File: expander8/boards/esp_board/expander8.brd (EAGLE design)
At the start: 68.6 x 46.7 mm, 63 parts, among them IC1 STM32F10XCXT6, IC2 78L05F, J1 DCJ0202

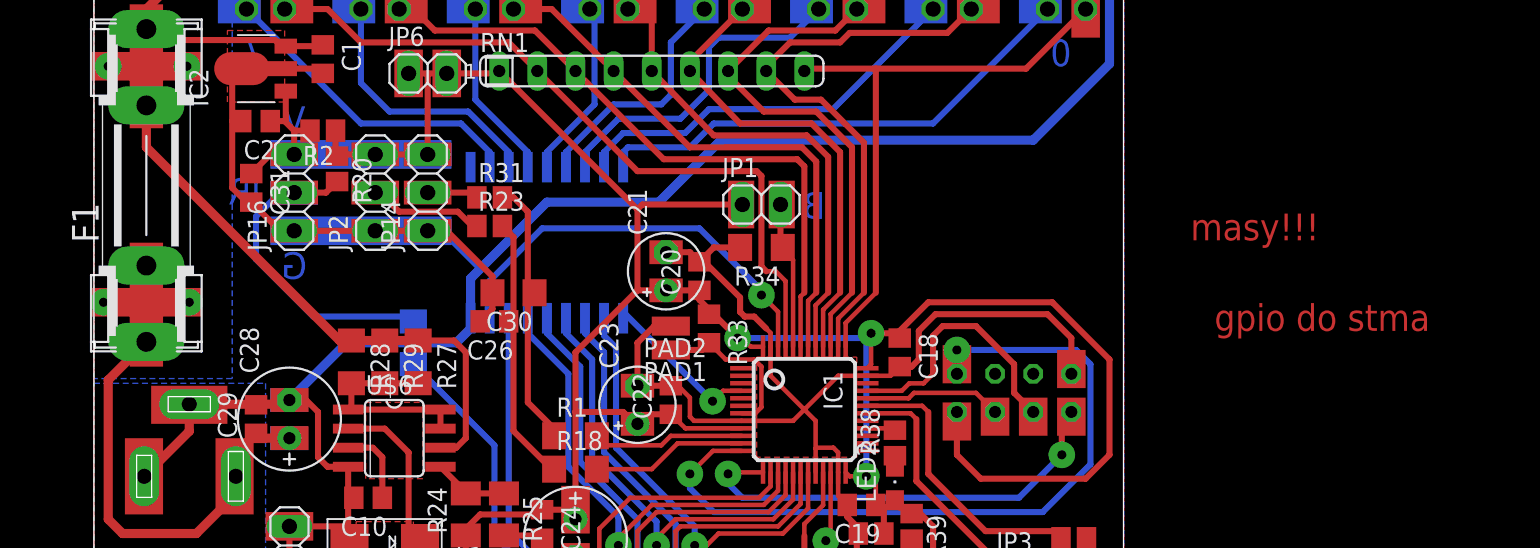
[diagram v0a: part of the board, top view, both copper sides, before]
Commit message: added ESP GPIO2 connection
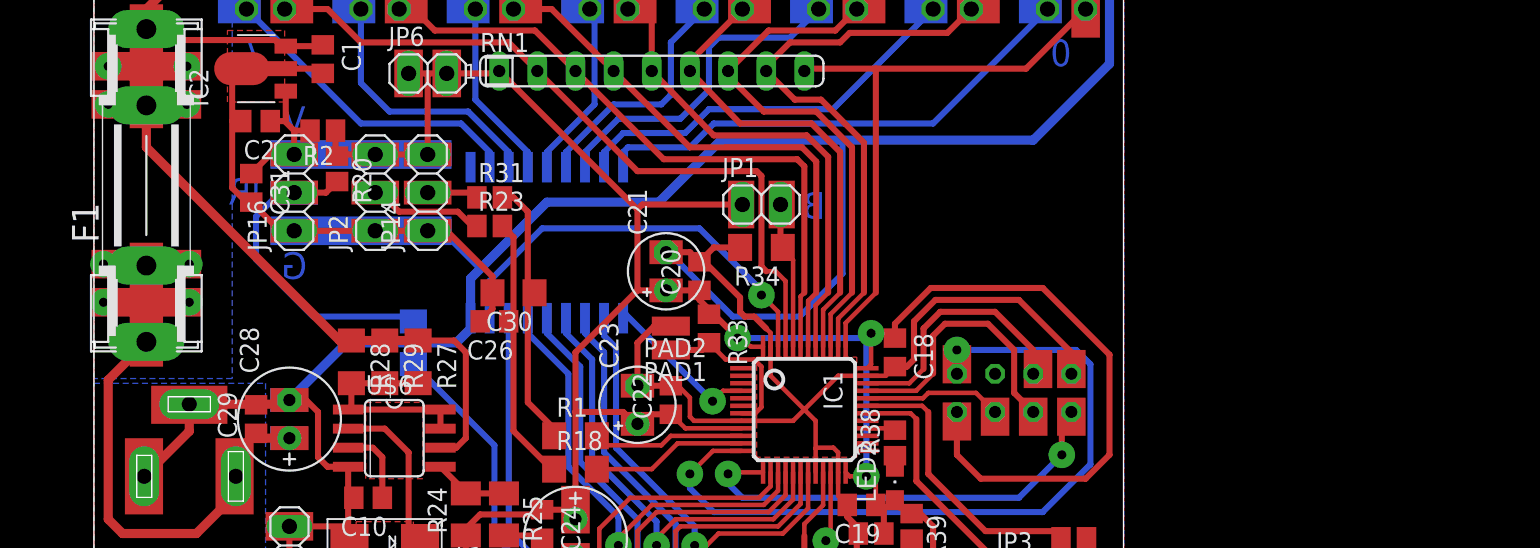
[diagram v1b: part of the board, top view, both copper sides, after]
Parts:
- moved C18 0.32 mm to (53.3, 37.0)
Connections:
- new net ESP_GPIO2: IC1.34, U$1.GPIO2
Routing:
- net GND: track 369.5 -> 393.7 mm
- net ESP_GPIO2: track 0.00 -> 17.2 mm
- net VCC: track 173.0 -> 174.7 mm
- net ESP_CH_PD: track 17.8 -> 18.5 mm
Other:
- board text removed: "gpio do stma"
- board text removed: "masy!!!"
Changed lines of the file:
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@@
 <circle x="81.28" y="69.85" radius="2.479753125" width="0.4064" layer="1"/>
 <circle x="81.28" y="69.85" radius="2.479753125" width="0.4064" layer="1"/>
-<text x="73.025" y="44.45" size="1.778" layer="1">masy!!!</text>
-<text x="74.6125" y="38.4175" size="1.778" layer="1">gpio do stma</text>
+<rectangle x1="61.9125" y1="34.6075" x2="63.8175" y2="37.1475" layer="1"/>
+<rectangle x1="-0.15875" y1="52.54625" x2="7.14375" y2="54.45125" layer="1"/>
+<rectangle x1="-0.15875" y1="41.91" x2="7.14375" y2="43.815" layer="1"/>
 </plain>
 <attributes>
@@
 <elements>
 <element name="IC1" library="stm32" package="TQFP48" value="STM32F10XCXT6" x="47.3075" y="33.17875" rot="R270"/>
-<element name="C18" library="rcl-kd" package="C0805" value="100n" x="53.6575" y="36.98875" rot="R270"/>
+<element name="C18" library="rcl-kd" package="C0805" value="100n" x="53.34" y="36.98875" rot="R270"/>
 <element name="C19" library="rcl-kd" package="C0805" value="100n" x="51.1175" y="26.82875" rot="R180"/>
 <element name="C20" library="rcl-kd" package="C0805" value="100n" x="40.3225" y="42.06875" rot="R90"/>
@@
 <wire x1="30.1625" y1="46.99" x2="37.62375" y2="46.99" width="0.6096" layer="16"/>
 <wire x1="37.62375" y1="46.99" x2="41.75125" y2="51.1175" width="0.6096" layer="16"/>
-<wire x1="41.75125" y1="51.1175" x2="62.5475" y2="51.1175" width="0.6096" layer="16"/>
+<wire x1="41.75125" y1="51.1175" x2="49.8475" y2="51.1175" width="0.6096" layer="16"/>
+<wire x1="49.8475" y1="51.1175" x2="62.5475" y2="51.1175" width="0.6096" layer="16"/>
 <wire x1="62.5475" y1="51.1175" x2="67.6275" y2="56.1975" width="0.6096" layer="16"/>
 <wire x1="67.6275" y1="56.1975" x2="67.6275" y2="61.595" width="0.6096" layer="16"/>
@@
 <contactref element="C27" pad="-"/>
 <contactref element="U$1" pad="GND"/>
-<wire x1="65.0875" y1="35.56" x2="65.0875" y2="37.94125" width="0.4064" layer="1"/>
-<wire x1="65.0875" y1="37.94125" x2="63.5" y2="39.52875" width="0.4064" layer="1"/>
-<wire x1="63.5" y1="39.52875" x2="56.03875" y2="39.52875" width="0.4064" layer="1"/>
-<wire x1="56.03875" y1="39.52875" x2="54.9275" y2="38.4175" width="0.4064" layer="1"/>
-<wire x1="54.9275" y1="38.4175" x2="54.9275" y2="36.5125" width="0.4064" layer="1"/>
-<wire x1="53.6575" y1="36.03875" x2="54.45375" y2="36.03875" width="0.4064" layer="1"/>
-<wire x1="54.45375" y1="36.03875" x2="54.9275" y2="36.5125" width="0.4064" layer="1"/>
-<wire x1="51.49" y1="35.42875" x2="53.0475" y2="35.42875" width="0.3048" layer="1"/>
-<wire x1="53.0475" y1="35.42875" x2="53.6575" y2="36.03875" width="0.3048" layer="1"/>
+<wire x1="65.0875" y1="35.56" x2="65.0875" y2="36.98875" width="0.4064" layer="1"/>
+<wire x1="65.0875" y1="36.98875" x2="61.595" y2="40.48125" width="0.4064" layer="1"/>
+<wire x1="61.595" y1="40.48125" x2="56.03875" y2="40.48125" width="0.4064" layer="1"/>
+<wire x1="56.03875" y1="40.48125" x2="54.61" y2="39.0525" width="0.4064" layer="1"/>
+<wire x1="54.61" y1="39.0525" x2="54.61" y2="36.5125" width="0.4064" layer="1"/>
+<wire x1="53.34" y1="36.03875" x2="54.13625" y2="36.03875" width="0.4064" layer="1"/>
+<wire x1="54.13625" y1="36.03875" x2="54.61" y2="36.5125" width="0.4064" layer="1"/>
+<wire x1="51.49" y1="35.42875" x2="52.73" y2="35.42875" width="0.3048" layer="1"/>
+<wire x1="52.73" y1="35.42875" x2="53.34" y2="36.03875" width="0.3048" layer="1"/>
 <wire x1="50.8" y1="22.06625" x2="50.8" y2="24.765" width="0.4064" layer="1"/>
 <wire x1="50.8" y1="24.765" x2="50.8" y2="25.4" width="0.4064" layer="1"/>
@@
 <wire x1="14.12875" y1="33.81375" x2="14.9225" y2="33.02" width="0.4064" layer="1"/>
 <wire x1="14.9225" y1="33.02" x2="14.9225" y2="30.00375" width="0.4064" layer="1"/>
+<wire x1="49.8475" y1="51.1175" x2="49.8475" y2="42.2275" width="0.4064" layer="16"/>
+<wire x1="49.8475" y1="42.2275" x2="46.99" y2="39.37" width="0.4064" layer="16"/>
+<wire x1="46.99" y1="39.37" x2="42.545" y2="39.37" width="0.4064" layer="16"/>
+<wire x1="42.545" y1="39.37" x2="38.4175" y2="43.4975" width="0.4064" layer="16"/>
+<wire x1="38.4175" y1="43.4975" x2="38.25875" y2="43.4975" width="0.4064" layer="16"/>
+<wire x1="38.25875" y1="43.4975" x2="38.1" y2="43.65625" width="0.4064" layer="16"/>
 </signal>
 <signal name="VCC">
@@
 <wire x1="59.055" y1="28.575" x2="66.04" y2="28.575" width="0.4064" layer="1"/>
 <wire x1="66.04" y1="28.575" x2="67.6275" y2="30.1625" width="0.4064" layer="1"/>
-<wire x1="67.6275" y1="30.1625" x2="67.6275" y2="36.5125" width="0.4064" layer="1"/>
-<wire x1="67.6275" y1="36.5125" x2="63.8175" y2="40.3225" width="0.4064" layer="1"/>
-<wire x1="63.8175" y1="40.3225" x2="55.5625" y2="40.3225" width="0.4064" layer="1"/>
-<wire x1="53.6575" y1="37.93875" x2="53.6575" y2="38.4175" width="0.4064" layer="1"/>
-<wire x1="53.6575" y1="38.4175" x2="55.5625" y2="40.3225" width="0.4064" layer="1"/>
+<wire x1="67.6275" y1="30.1625" x2="67.6275" y2="36.83" width="0.4064" layer="1"/>
+<wire x1="63.1825" y1="41.275" x2="55.72125" y2="41.275" width="0.4064" layer="1"/>
+<wire x1="53.34" y1="37.93875" x2="53.34" y2="38.89375" width="0.4064" layer="1"/>
+<wire x1="53.34" y1="38.89375" x2="55.72125" y2="41.275" width="0.4064" layer="1"/>
 <wire x1="51.7525" y1="38.25875" x2="53.49875" y2="38.25875" width="0.4064" layer="1"/>
-<wire x1="53.49875" y1="38.25875" x2="53.6575" y2="38.4175" width="0.4064" layer="1"/>
 <wire x1="52.22625" y1="26.67" x2="52.0675" y2="26.82875" width="0.4064" layer="1"/>
 <wire x1="52.22625" y1="26.67" x2="52.705" y2="26.67" width="0.4064" layer="1"/>
@@
 <wire x1="53.34" y1="27.2075" x2="53.34" y2="26.9875" width="0.4064" layer="1"/>
 <wire x1="53.34" y1="26.9875" x2="53.6575" y2="26.67" width="0.4064" layer="1"/>
+<wire x1="53.49875" y1="38.25875" x2="53.49875" y2="38.0975" width="0.4064" layer="1"/>
+<wire x1="53.49875" y1="38.0975" x2="53.34" y2="37.93875" width="0.4064" layer="1"/>
 <wire x1="15.875" y1="50.165" x2="11.75" y2="50.165" width="0" layer="19" extent="1-1"/>
+<wire x1="63.1825" y1="41.275" x2="67.6275" y2="36.83" width="0.4064" layer="1"/>
 </signal>
 <signal name="VBAT">
@@
 <signal name="ESP_RST">
 <contactref element="IC1" pad="32"/>
-<wire x1="51.49" y1="33.92875" x2="54.24875" y2="33.92875" width="0.3048" layer="1"/>
-<wire x1="54.24875" y1="33.92875" x2="54.61" y2="34.29" width="0.3048" layer="1"/>
-<wire x1="54.61" y1="34.29" x2="58.7375" y2="34.29" width="0.3048" layer="1"/>
+<wire x1="51.49" y1="33.92875" x2="55.20125" y2="33.92875" width="0.3048" layer="1"/>
+<wire x1="55.20125" y1="33.92875" x2="55.5625" y2="34.29" width="0.3048" layer="1"/>
+<wire x1="55.5625" y1="34.29" x2="58.7375" y2="34.29" width="0.3048" layer="1"/>
 <contactref element="U$1" pad="RST"/>
 <wire x1="58.7375" y1="34.29" x2="60.0075" y2="33.02" width="0.3048" layer="1"/>
@@
 <contactref element="IC1" pad="33"/>
 <contactref element="U$1" pad="CH_PD"/>
-<wire x1="51.49" y1="34.42875" x2="53.79625" y2="34.42875" width="0.3048" layer="1"/>
-<wire x1="53.79625" y1="34.42875" x2="54.2925" y2="34.925" width="0.3048" layer="1"/>
-<wire x1="54.2925" y1="34.925" x2="55.245" y2="34.925" width="0.3048" layer="1"/>
-<wire x1="55.245" y1="34.925" x2="55.88" y2="35.56" width="0.3048" layer="1"/>
+<wire x1="51.49" y1="34.42875" x2="54.74875" y2="34.42875" width="0.3048" layer="1"/>
+<wire x1="54.74875" y1="34.42875" x2="55.88" y2="35.56" width="0.3048" layer="1"/>
 <wire x1="55.88" y1="35.56" x2="55.88" y2="38.1" width="0.4064" layer="1"/>
-<wire x1="55.88" y1="38.1" x2="56.515" y2="38.735" width="0.4064" layer="1"/>
-<wire x1="56.515" y1="38.735" x2="58.7375" y2="38.735" width="0.4064" layer="1"/>
-<wire x1="58.7375" y1="38.735" x2="61.2775" y2="36.195" width="0.4064" layer="1"/>
-<wire x1="61.2775" y1="36.195" x2="61.2775" y2="34.29" width="0.4064" layer="1"/>
+<wire x1="55.88" y1="38.1" x2="56.67375" y2="38.89375" width="0.4064" layer="1"/>
+<wire x1="56.67375" y1="38.89375" x2="59.53125" y2="38.89375" width="0.4064" layer="1"/>
+<wire x1="59.53125" y1="38.89375" x2="61.2775" y2="37.1475" width="0.4064" layer="1"/>
+<wire x1="61.2775" y1="37.1475" x2="61.2775" y2="34.29" width="0.4064" layer="1"/>
 <wire x1="61.2775" y1="34.29" x2="62.5475" y2="33.02" width="0.4064" layer="1"/>
 </signal>
@@
 <signal name="N$1">
 <via x="0.635" y="40.3225" extent="1-16" drill="0.6" diameter="1.778" shape="square"/>
+<via x="0.635" y="42.8625" extent="1-16" drill="0.6" diameter="1.778" shape="square"/>
 </signal>
 <signal name="N$2">
 <via x="6.35" y="40.3225" extent="1-16" drill="0.6" diameter="1.778" shape="square"/>
+<via x="6.35" y="42.8625" extent="1-16" drill="0.6" diameter="1.778" shape="square"/>
 </signal>
 <signal name="N$6">
 <via x="0.9525" y="56.03875" extent="1-16" drill="0.6" diameter="1.778" shape="square"/>
+<via x="0.9525" y="53.49875" extent="1-16" drill="0.6" diameter="1.778" shape="square"/>
 </signal>
 <signal name="N$7">
 <via x="6.19125" y="56.03875" extent="1-16" drill="0.6" diameter="1.778" shape="square"/>
+<via x="6.19125" y="53.49875" extent="1-16" drill="0.6" diameter="1.778" shape="square"/>
 </signal>
 <signal name="N$9">
@@
 <wire x1="78.74" y1="69.85" x2="83.82" y2="69.85" width="0.4064" layer="1"/>
 </signal>
+<signal name="ESP_GPIO2">
+<contactref element="IC1" pad="34"/>
+<contactref element="U$1" pad="GPIO2"/>
+<wire x1="51.49" y1="34.92875" x2="54.29625" y2="34.92875" width="0.3048" layer="1"/>
+<wire x1="54.29625" y1="34.92875" x2="55.245" y2="35.8775" width="0.3048" layer="1"/>
+<wire x1="55.245" y1="35.8775" x2="55.245" y2="38.57625" width="0.4064" layer="1"/>
+<wire x1="55.245" y1="38.57625" x2="56.35625" y2="39.6875" width="0.4064" layer="1"/>
+<wire x1="56.35625" y1="39.6875" x2="60.0075" y2="39.6875" width="0.4064" layer="1"/>
+<wire x1="60.0075" y1="39.6875" x2="62.5475" y2="37.1475" width="0.4064" layer="1"/>
+<wire x1="62.5475" y1="37.1475" x2="62.5475" y2="35.56" width="0.4064" layer="1"/>
+</signal>
 </signals>

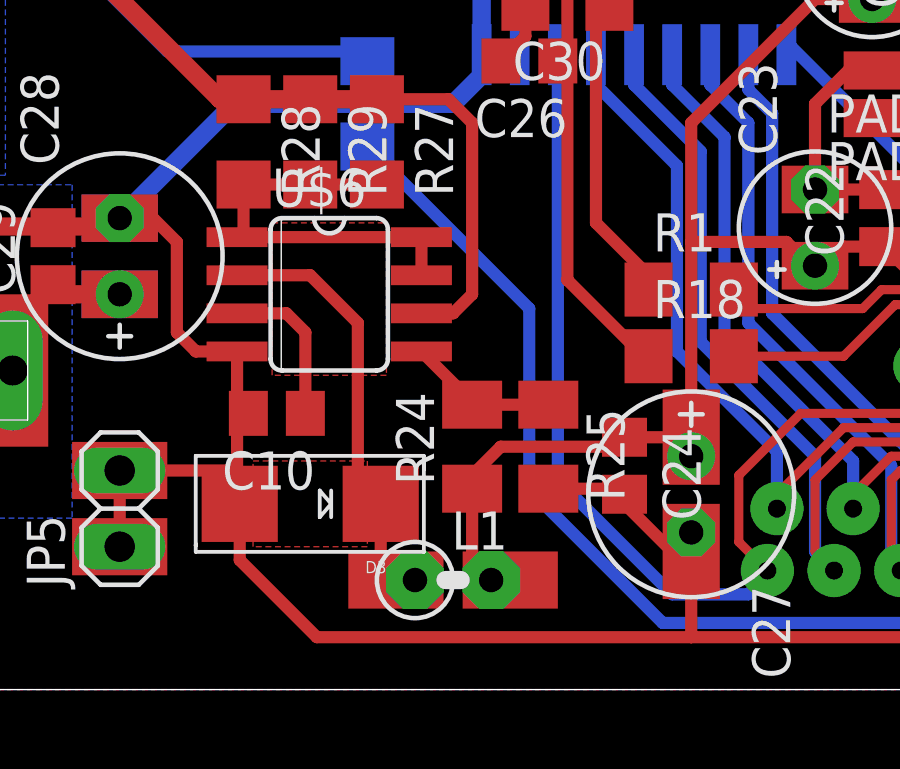
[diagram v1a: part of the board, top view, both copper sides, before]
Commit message: boards: added vcc polygon under dcdc
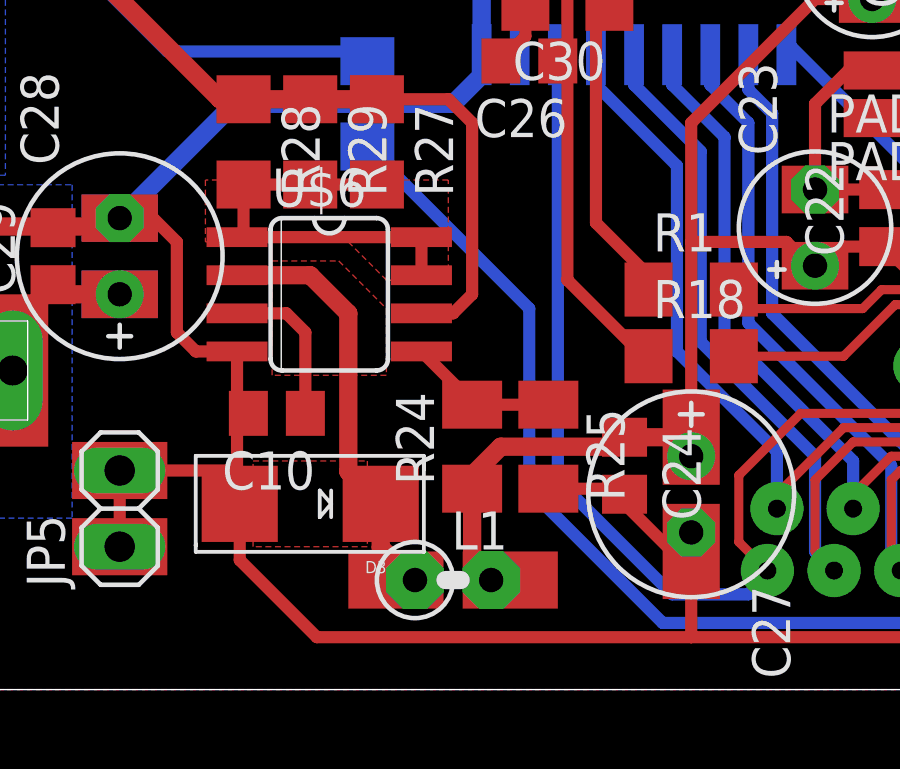
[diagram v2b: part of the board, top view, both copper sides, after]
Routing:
- net N$51: track 14.6 -> 14.1 mm
- added copper zone on layer 1, net IPK

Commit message: update
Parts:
- removed C24: 100n, rcl-kd:C0805
- removed F1: (no value), fuse:SHK20L
- removed PAD1, PAD2: (no value), wirepad:SMD1,27-2,54
- removed R21: 1M, rcl-kd:R1206
- removed R24: 360, rcl:M1206
- removed R27, R28, R29: 1, rcl-kd:R1206
- removed R30: 4k7, resistor:R0805
- removed U$6: MC33063/MC34063D, adafruit:SO08
- added C11, C12, C13, C15, C16, C4, C5, C6, C7, C8, C9: 100n, rcl-kd:C0805
- added C3: 10n, rcl-kd:C1206
- added IC5: (no value), SparkFun:SOT223
- added JP17: (no value), pinhead:1X02
- added R10, R12, R13, R14, R15, R16, R17, R19, R22, R9: 0, resistor:R0805
- added R11, R4, R5: 4k7, resistor:R0805
- added R3: 0, rcl:M1206
- added R35: (no value), resistor:R1206
- added R36: (no value), resistor:R0805
- added R8: 220, resistor:R1206
- added S1: (no value), switch-omron:B3F-10XX
- added U$2: USB-MINIB-5PIN, SparkFun:USB-MINIB
- added U$3: FT230XQ, ftdi_ft231xq-r2:FT230XQ
- added U$4: DS1820TO92, Ava_ds18:DS1820
- C10: value 220p -> 100n
- C30: device rcl-kd:C1206 -> rcl-kd:C0805
- C31: device rcl-kd:C0805 -> rcl-kd:C1206
- IC2: value 78L05F -> (none); device linear:SOT89 -> lm2674:SO8
- JP1: device pinhead-kd:1X02 -> pinhead:1X02
- JP3: device pinhead:1X03 -> pinhead-kd:1X02
- R2: value 0 -> 4k7; device resistor:R0805 -> rcl-kd:R0805
- R25: value 220 -> 4k7; device rcl:M1206 -> resistor:R0805
- R31: device resistor:R0805 -> resistor:R1206
- R34: device rcl-kd:R1206 -> rcl-kd:R0805
- moved R2 53.2 mm to (59.1, 21.6), turned to 0 degrees
- moved C10 39.4 mm to (38.4, 61.1), turned to 90 degrees
- moved JP3 37.3 mm to (26.7, 20.6), turned to 180 degrees
- moved JP1 32.1 mm to (19.7, 26.4)
- moved JP14 23.9 mm to (3.81, 62.9), turned to 180 degrees
- moved C30 23.4 mm to (8.89, 54.6), turned to 270 degrees
- moved R31 22.1 mm to (6.35, 56.7)
- moved C26 20.4 mm to (12.1, 53.3), flipped to the bottom, turned to 90 degrees
- moved JP2 19.0 mm to (3.81, 59.4), turned to 180 degrees
- moved D3 18.6 mm to (9.21, 39.8), turned to 0 degrees
- moved R23 17.6 mm to (10.2, 52.4), flipped to the bottom, turned to 180 degrees
- moved L1 16.8 mm to (12.1, 33.5), turned to 180 degrees
- moved R20 15.9 mm to (2.22, 56.8), turned to 0 degrees
- moved C27 14.5 mm to (19.7, 32.2)
- moved LED2 12.1 mm to (65.4, 27.3), turned to 180 degrees
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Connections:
- removed net COMP: R24.2, R25.1, U$6.5
- removed net CS: IC1.29
- removed net INT: IC1.25
- removed net IPK: R27.2, R28.2, R29.2, U$6.1, U$6.7, U$6.8
- removed net MISO: IC1.27
- removed net N$51: D3.C, L1.1, U$6.2
- removed net N$56: C10.1, U$6.3
- removed net N$57: C28.+, C29.1, F1.1A, J1.1
- removed net N$9: C2.1, IC2.1, JP16.3, R2.2
- removed net SCK: IC1.26
- new net AN_LIGHT: IC1.14, R8.1
- new net AN_LIGHT2: C7.1, JP3.2, R25.2, R8.2
- new net BTN1: IC1.27, R2.2, S1.1
- new net ESP_GPIO0: IC1.32, U$1.GPIO0
- new net IN1_: C13.1, JP4.1, R12.1, RN1.9
- new net IN2_: C16.1, JP7.1, R13.1, RN1.8
- new net IN3_: C12.1, JP8.1, R14.1, RN1.7
- new net IN4_: C11.1, JP9.1, R15.1, RN1.6
- new net IN5_: C10.1, JP10.1, R16.1, RN1.5
- new net IN6_: C9.1, JP11.1, R17.1, R9.1
- new net IN7_: C8.1, JP12.1, R10.1, R19.1
- new net IN8_: C1.1, JP13.1, R11.1, R22.1
- new net N$1: C3.2, D3.C, IC2.8, L1.2
- new net N$12: R9.2, RN1.4
- new net N$14: R10.2, RN1.3
- new net N$15: R11.2, RN1.2
- new net N$2: IC2.4, R4.1, R5.1
- new net N$38: R35.1, U$2.D-
- new net N$39: R35.2, U$3.7
- new net N$40: R36.2, U$3.6
- new net N$41: R36.1, U$2.D+
- new net N$6: C3.1, IC2.1
- new net N$7: J1.1, R3.1
- new net VCC_5V: C2.1, C27.+, C4.1, C6.1, IC5.3, JP1.1, JP1.2, JP16.3, L1.1, R20.1, R4.2
- new net VCC_USB: U$2.VBUS
- net ESP_RST: now also IC1.29; no longer IC1.32
- net GND: now also C11.2, C12.2, C13.2, C15.2, C16.2, C4.2, C5.2, C6.2, C7.2, C8.2, C9.2, IC2.6, IC5.1, R25.1, R5.2, S1.3, U$2.GND, U$3.12, U$3.13, U$3.3, U$3.C, U$4.GND; no longer C24.2, IC2.2, IC2.2@1, JP3.3, PAD2.1, R25.2, R30.1, U$6.4
- net IN1: now also R12.2; no longer JP4.1, RN1.9
- net IN2: now also R13.2; no longer JP7.1, RN1.8
- net IN3: now also R14.2; no longer JP8.1, RN1.7
- net IN4: now also R15.2; no longer JP9.1, RN1.6
- net IN5: now also R16.2; no longer JP10.1, RN1.5
- net IN6: now also R17.2; no longer JP11.1, RN1.4
- net IN7: now also R19.2; no longer JP12.1, RN1.3
- net IN8: now also R22.2; no longer JP13.1, RN1.2
- net N$64: now also JP17.2; no longer JP1.2
- net OUT7: now also IC1.25; no longer IC1.14
- net OW: now also U$4.DQ
- net RST1: no longer PAD1.1
- net RX: now also U$3.15; no longer JP3.2, R30.2
- net TX: now also U$3.2; no longer JP3.1
- net VCC: now also C15.1, C5.1, IC5.4, JP17.1, JP3.1, U$3.1, U$3.10, U$3.8, U$3.9, U$4.VDD; no longer C24.1, C27.+, JP1.1, L1.2, R20.1, R24.1
- net VCC_12V: now also C28.+, C29.1, IC2.7, R3.2; no longer C1.1, F1.2A, IC2.3, R27.1, R28.1, R29.1, U$6.6
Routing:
- net VCC_5V: track 0.00 -> 79.1 mm, vias 0 -> 2
- net GND: track 393.7 -> 470.2 mm, vias 0 -> 4
- net VCC: track 174.7 -> 249.2 mm, vias 3 -> 4
- net N$57: track 29.8 -> 0.00 mm
- net IN8_: track 0.00 -> 26.7 mm
- net AN1: track 29.0 -> 55.2 mm, vias 0 -> 2
- net IN1_: track 0.00 -> 25.7 mm
- net IN8: track 48.8 -> 25.6 mm
- net IN2_: track 0.00 -> 23.1 mm
- net VCC_12V: track 131.6 -> 109.5 mm, vias 0 -> 2
- net IN1: track 39.8 -> 18.0 mm
- net IN7_: track 0.00 -> 21.3 mm
- net ESP_RST: track 9.19 -> 28.3 mm
- net IN2: track 38.3 -> 19.3 mm
- net IN7: track 43.4 -> 24.8 mm
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- added copper zone on layer 16, net BTN1
- removed copper zone on layer 1, net IPK
- removed copper zone on layer 1, net N$30
- removed copper zone on layer 16, net N$4
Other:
- board text added: "1"
- board text added: "2"
- board text added: "3"
- board text added: "3V3"
- board text added: "4"
- board text added: "5"
- board text added: "5V"
- board text added: "6"
- board text added: "BOOT"
- board text added: "GND"
- board text added: "LIGHT"
- board text removed: "B"
- board text removed: "R"
- board text removed: "T"
